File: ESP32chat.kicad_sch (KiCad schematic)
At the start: 181 parts, among them J1 CONN_021X02_NO_SILK, J2 CONN_01, J3 CONN_01, J4 CONN_021X02_NO_SILK, J5 CONN_021X02_NO_SILK, J6 CONN_021X02_NO_SILK, Q1 Q_PMOS_DGS, Q2 BSS123, Q3 Si1308, SW1 SW_DIP_x01, U1 MCP73831T-2ACI/OT, U10 MOUNTINGHOLE2.0, U11 MOUNTINGHOLE2.0, U12 MOUNTINGHOLE2.0, U13 MOUNTINGHOLE2.0, U14 MOUNTINGHOLE2.0, U15 MOUNTINGHOLE2.0, U16 MB85RC64, U17 MOUNTINGHOLE2.0, U18 MOUNTINGHOLE2.0, U19 BGU8019, U2 TP4056, U20 LM75B, U21 ATGM336H-5N31, U22 QMC5883L, U23 FPCConn, U3 ESP32, U4 FS8205A, U5 DW01, U6 RT9013, U7 RFM69HCW, U8 tp4056_KoreanHropartsElecTYPE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, U9 BUZZER, X1 uFL

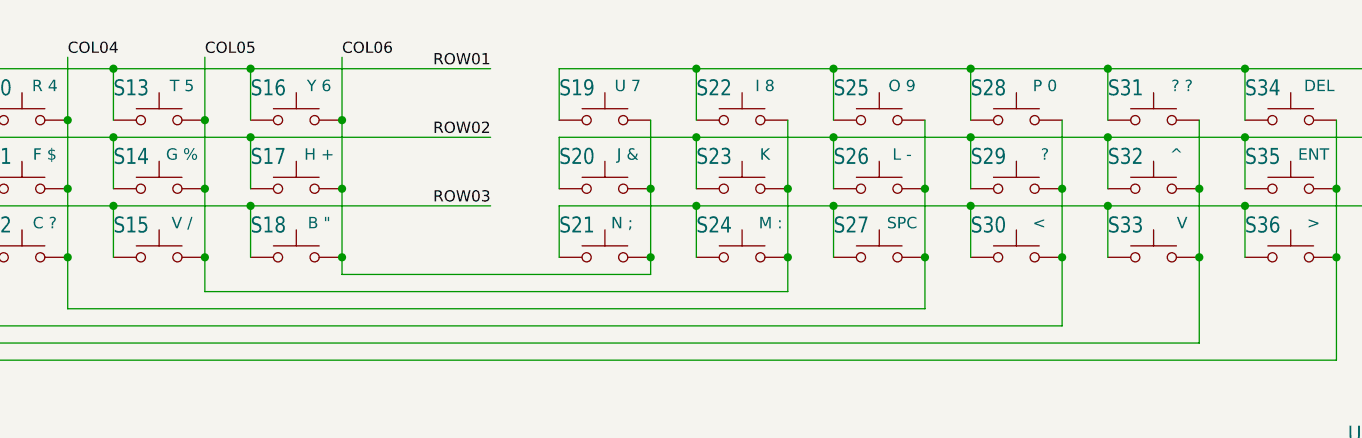
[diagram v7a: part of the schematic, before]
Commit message: Updated kepad layout
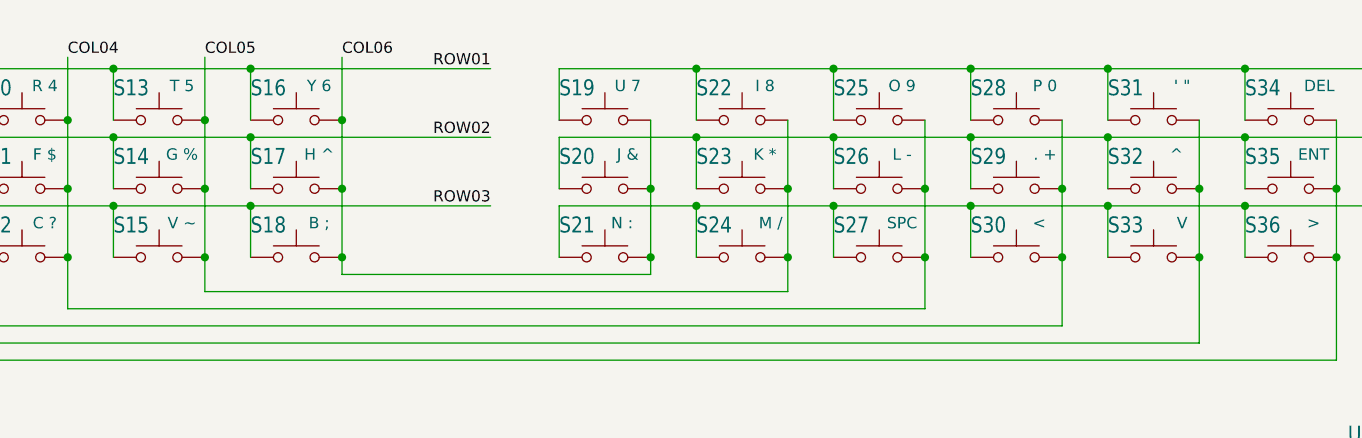
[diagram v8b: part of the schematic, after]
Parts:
- S15: Field5 V / -> V ~
- S17: Field5 H + -> H ^
- S18: Field5 B " -> B ;
- S21: Field5 N ; -> N :
- S23: Field5 K -> K *
- S24: Field5 M : -> M /
- S29: Field5 ? -> . +
- S31: Field5 ? ? -> ' "
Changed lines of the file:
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@@
       (effects (font (size 1.27 1.27)) hide)
     )
-    (property "Field5" "N ;" (id 5) (at 139.065 37.465 0))
+    (property "Field5" "N :" (id 5) (at 139.065 37.465 0))
     (pin "1")
     (pin "2")
@@
       (effects (font (size 1.27 1.27)) hide)
     )
-    (property "Field5" "? ?" (id 5) (at 201.295 22.225 0))
+    (property "Field5" "' \"" (id 5) (at 201.295 22.225 0))
     (pin "1")
     (pin "2")
@@
       (effects (font (size 1.27 1.27)) hide)
     )
-    (pin "6")
-    (pin "7")
     (pin "1")
-    (pin "3")
     (pin "2")
+    (pin "3")
     (pin "4")
-    (pin "8")
     (pin "5")
+    (pin "6")
+    (pin "7")
+    (pin "8")
   )
   (symbol (lib_id "Switch:SW_Push") (at 213.36 26.035 0) (unit 1)
@@
       (effects (font (size 1.27 1.27)) hide)
     )
-    (property "Field5" "B \"" (id 5) (at 105.41 37.465 0))
+    (property "Field5" "B ;" (id 5) (at 105.41 37.465 0))
     (pin "1")
     (pin "2")
@@
       (effects (font (size 1.27 1.27)) hide)
     )
-    (property "Field5" "?" (id 5) (at 186.055 29.845 0))
+    (property "Field5" ". +" (id 5) (at 186.055 29.845 0))
     (pin "1")
     (pin "2")
@@
       (effects (font (size 1.27 1.27)) hide)
     )
-    (property "Field5" "K " (id 5) (at 154.94 29.845 0))
+    (property "Field5" "K *" (id 5) (at 154.94 29.845 0))
     (pin "1")
     (pin "2")
@@
       (effects (font (size 1.27 1.27)) hide)
     )
-    (property "Field5" "M :" (id 5) (at 155.575 37.465 0))
+    (property "Field5" "M /" (id 5) (at 155.575 37.465 0))
     (pin "1")
     (pin "2")
@@
       (effects (font (size 1.27 1.27)) hide)
     )
-    (property "Field5" "V /" (id 5) (at 90.17 37.465 0))
+    (property "Field5" "V ~" (id 5) (at 90.17 37.465 0))
     (pin "1")
     (pin "2")
@@
       (effects (font (size 1.27 1.27)) hide)
     )
-    (property "Field5" "H +" (id 5) (at 105.41 29.845 0))
+    (property "Field5" "H ^" (id 5) (at 105.41 29.845 0))
     (pin "1")
     (pin "2")
